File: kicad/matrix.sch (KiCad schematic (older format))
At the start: 6 parts

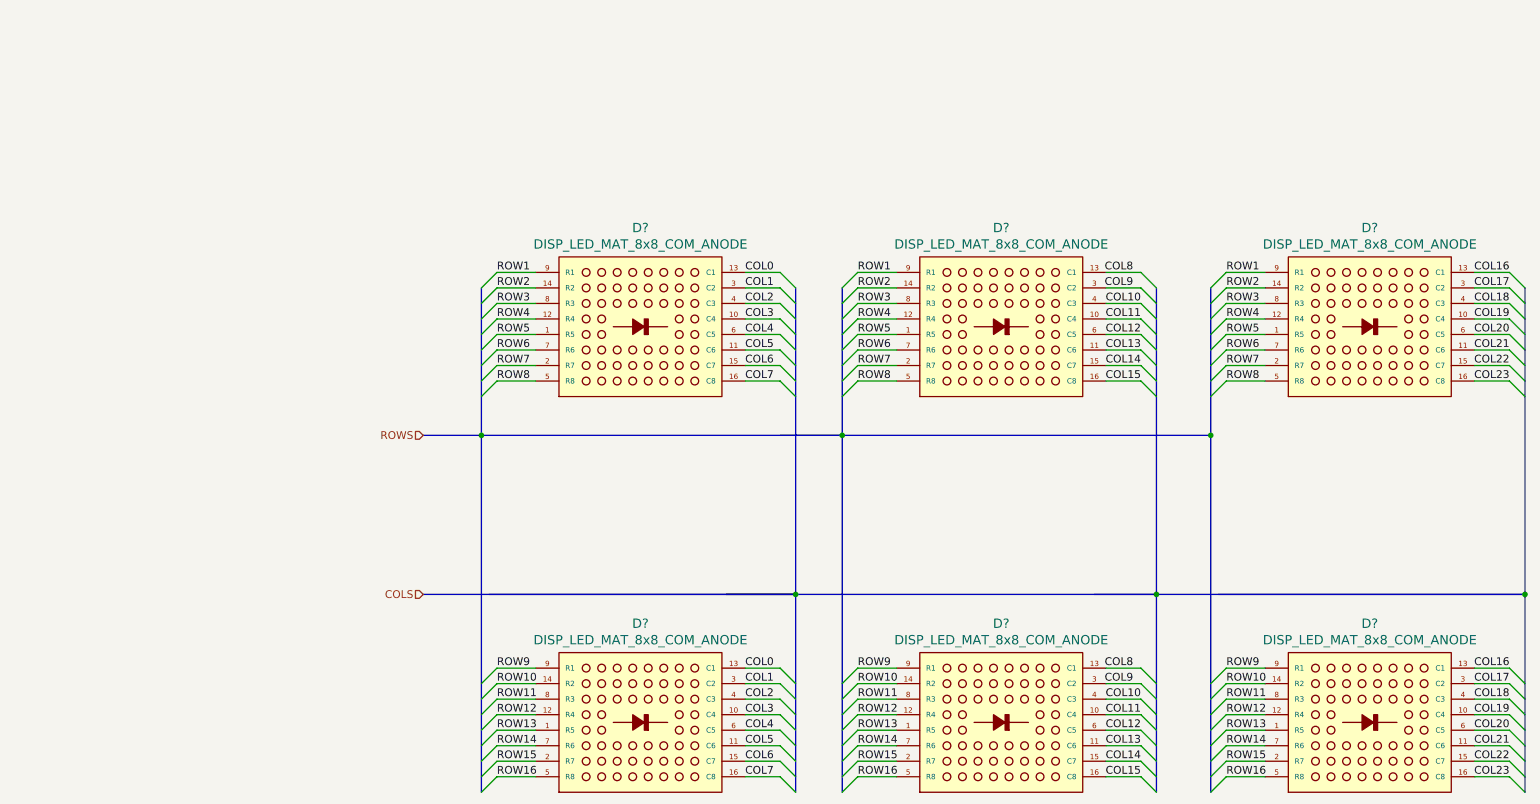
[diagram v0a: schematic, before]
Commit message: Clean up DRC errors and buses
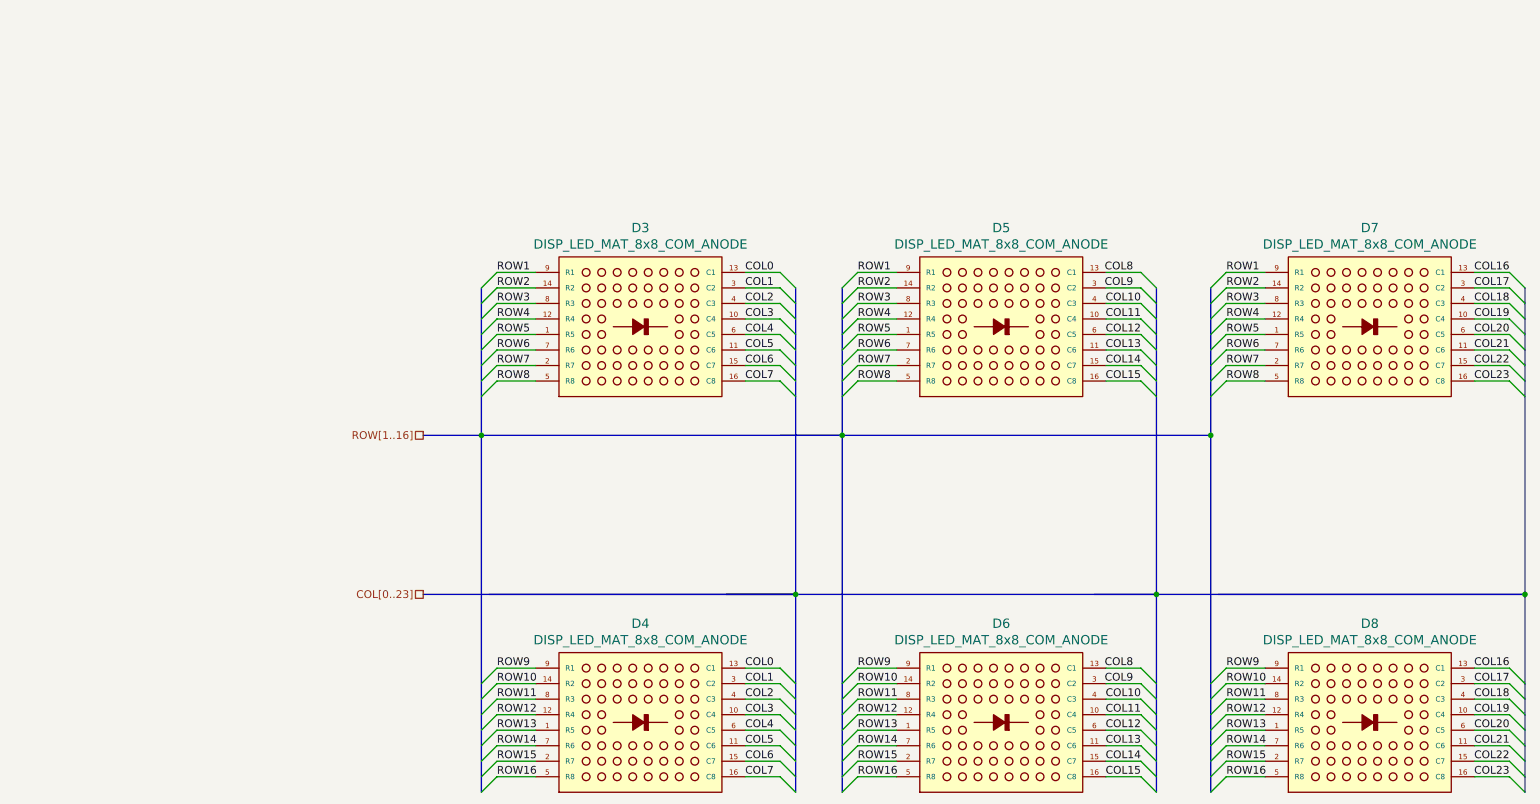
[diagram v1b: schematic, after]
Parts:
- gave numbers to parts that had none: 6
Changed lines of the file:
@@
 P 2825 3275
 AR Path="/5F65D5AA" Ref="D?"  Part="1"
-AR Path="/5F613F5E/5F65D5AA" Ref="D?"  Part="1"
-F 0 "D?" H 3500 4362 60  0000 C CNN
+AR Path="/5F613F5E/5F65D5AA" Ref="D3"  Part="1"
+F 0 "D3" H 3500 4362 60  0000 C CNN
 F 1 "DISP_LED_MAT_8x8_COM_ANODE" H 3500 4256 60  0000 C CNN
 F 2 "local:LED_8x8_3MM_38x38MM" H 2925 3225 60  0001 C CNN
@@
 P 5150 3275
 AR Path="/5F65D5B0" Ref="D?"  Part="1"
-AR Path="/5F613F5E/5F65D5B0" Ref="D?"  Part="1"
-F 0 "D?" H 5825 4362 60  0000 C CNN
+AR Path="/5F613F5E/5F65D5B0" Ref="D5"  Part="1"
+F 0 "D5" H 5825 4362 60  0000 C CNN
 F 1 "DISP_LED_MAT_8x8_COM_ANODE" H 5825 4256 60  0000 C CNN
 F 2 "local:LED_8x8_3MM_38x38MM" H 5250 3225 60  0001 C CNN
@@
 P 2825 5825
 AR Path="/5F65D5B6" Ref="D?"  Part="1"
-AR Path="/5F613F5E/5F65D5B6" Ref="D?"  Part="1"
-F 0 "D?" H 3500 6912 60  0000 C CNN
+AR Path="/5F613F5E/5F65D5B6" Ref="D4"  Part="1"
+F 0 "D4" H 3500 6912 60  0000 C CNN
 F 1 "DISP_LED_MAT_8x8_COM_ANODE" H 3500 6806 60  0000 C CNN
 F 2 "local:LED_8x8_3MM_38x38MM" H 2925 5775 60  0001 C CNN
@@
 P 5150 5825
 AR Path="/5F65D5BC" Ref="D?"  Part="1"
-AR Path="/5F613F5E/5F65D5BC" Ref="D?"  Part="1"
-F 0 "D?" H 5825 6912 60  0000 C CNN
+AR Path="/5F613F5E/5F65D5BC" Ref="D6"  Part="1"
+F 0 "D6" H 5825 6912 60  0000 C CNN
 F 1 "DISP_LED_MAT_8x8_COM_ANODE" H 5825 6806 60  0000 C CNN
 F 2 "local:LED_8x8_3MM_38x38MM" H 5250 5775 60  0001 C CNN
@@
 P 7525 3275
 AR Path="/5F65D689" Ref="D?"  Part="1"
-AR Path="/5F613F5E/5F65D689" Ref="D?"  Part="1"
-F 0 "D?" H 8200 4362 60  0000 C CNN
+AR Path="/5F613F5E/5F65D689" Ref="D7"  Part="1"
+F 0 "D7" H 8200 4362 60  0000 C CNN
 F 1 "DISP_LED_MAT_8x8_COM_ANODE" H 8200 4256 60  0000 C CNN
 F 2 "local:LED_8x8_3MM_38x38MM" H 7625 3225 60  0001 C CNN
@@
 P 7525 5825
 AR Path="/5F65D68F" Ref="D?"  Part="1"
-AR Path="/5F613F5E/5F65D68F" Ref="D?"  Part="1"
-F 0 "D?" H 8200 6912 60  0000 C CNN
+AR Path="/5F613F5E/5F65D68F" Ref="D8"  Part="1"
+F 0 "D8" H 8200 6912 60  0000 C CNN
 F 1 "DISP_LED_MAT_8x8_COM_ANODE" H 8200 6806 60  0000 C CNN
 F 2 "local:LED_8x8_3MM_38x38MM" H 7625 5775 60  0001 C CNN
@@
 Wire Bus Line
 	2475 3525 2100 3525
+Text HLabel 2100 3525 0    50   UnSpc ~ 0
+ROW[1..16]
+Text HLabel 2100 4550 0    50   UnSpc ~ 0
+COL[0..23]
 Wire Bus Line
 	7175 3525 7175 5825
@@
 Wire Bus Line
 	2475 3525 2475 5825
-Text HLabel 2100 3525 0    50   Input ~ 0
-ROWS
-Text HLabel 2100 4550 0    50   Input ~ 0
-COLS
 $EndSCHEMATC

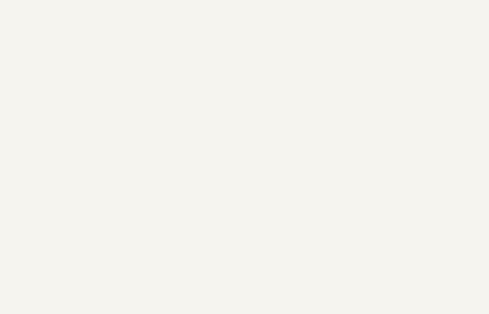
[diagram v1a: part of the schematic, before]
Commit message: Finishes matrix driver circuit
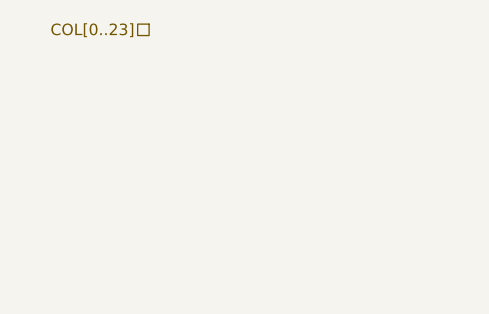
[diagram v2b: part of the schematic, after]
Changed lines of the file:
@@
 $Descr A4 11693 8268
 encoding utf-8
-Sheet 3 3
+Sheet 3 4
 Title ""
 Date ""
@@
 Text HLabel 2100 4550 0    50   UnSpc ~ 0
 COL[0..23]
-Wire Bus Line
+Text HLabel 25   850  0    50   UnSpc ~ 0
+COL[0..23]
+Wire Bus Line
